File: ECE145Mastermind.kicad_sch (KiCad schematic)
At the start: 17 parts, among them U1 74LS148, U10 74LS76, U11 74LS76, U13 4053, U14 4053, U15 4051, U16 74LS161, U17 74HC00, U19 74HC00, U2 74LS194, U20 74HC00, U21 74LS139, U22 74LS08, U24 LM555xN, U26 74LS04, U29 74LS194, U30 74LS194

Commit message: Added FSM, Button, 555 timer, changed shift registers
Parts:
- added C1, C4: .01u, symbol Device:C
- added C2, C3: 1u, symbol Device:C
- added Q1: NMOS, symbol Simulation_SPICE:NMOS
- added R1: 1k, symbol Device:R
- added R2: 200k, symbol Device:R
- added R3, R4: R, symbol Device:R
- added SW1: SW_Push, symbol Switch:SW_Push
- added unit 5 of U1
- added unit 1 of U14
- added unit 5 of U14
- added U17: 40106, symbol 4xxx:40106
- added unit 3 of U2
- added U5: 74LS08, symbol 74xx:74LS08
- added unit 3 of U6
- added unit 3 of U8
- added unit 7 of U9
- U1: renamed from U20; value 74HC00 -> 74HCT00; symbol 74xx:74HC00 -> 74xx:74HCT00
- U1: renamed from U17; value 74HC00 -> 74HCT00; symbol 74xx:74HC00 -> 74xx:74HCT00
- U1: renamed from U19; value 74HC00 -> 74HCT00; symbol 74xx:74HC00 -> 74xx:74HCT00
- U15: renamed from U24; Name (none) -> 555 Timer
- U9: renamed from U26; value 74LS04 -> 74HCT04; symbol 74xx:74LS04 -> 74xx:74HCT04
- renumbered U13 to U10, U30 to U11, U14 to U12, U15 to U13, U22 to U14, U11 to U2, U29 to U3, U1 to U4, U10 to U6, U2 to U7, U21 to U8
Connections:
- net GND is gone; now on net +5V: U10.7 (VEE), U10.8 (VSS), U12.7 (VEE), U12.8 (VSS), U13.7 (VEE), U13.8 (VSS), U16.8 (GND), U4.8 (GND)
- net MUX.S is gone; now on net M: U10.10 (B), U10.11 (A), U10.9 (C), U12.9 (C)
- net Reset is gone; now on net GUESS: U2.2 (~{S}), U2.7 (~{S}), U6.2 (~{S}), U6.7 (~{S})
- net +5V: now also U10.6 (Inh), U11.10 (S1), U11.16 (VCC), U11.7 (Dsl), U11.8 (GND), U12.10 (B), U12.11 (A), U12.6 (Inh), U13.6 (Inh), U13.9 (C), U15.1 (GND), U15.4 (R), U15.8 (VCC), U16.10 (CET), U16.7 (CEP), U16.9 (~{PE}), U2.3 (~{R}), U2.4 (J), U2.8 (~{R}), U2.9 (J), U3.10 (S1), U3.16 (VCC), U3.8 (GND), U4.1 (I4), U4.2 (I5), U4.3 (I6), U4.4 (I7), U4.5 (EI), U6.3 (~{R}), U6.4 (J), U6.8 (~{R}), U6.9 (J), U7.10 (S1), U7.16 (VCC), U7.2 (Dsr), U7.8 (GND), C1.2, C2.2, C4.1, Q1.3 (S), R1.1, R3.1, R4.1, SW1.2, U1.14 (VCC), U1.7 (GND), U14.14 (VCC), U14.7 (GND), U17.14 (VDD), U17.7 (VSS), U2.13 (GND), U2.5 (VCC), U5.14 (VCC), U5.7 (GND), U6.13 (GND), U6.5 (VCC), U8.16 (VCC), U8.8 (GND), U9.14 (VCC), U9.7 (GND)
- net CLK: now also U11.11 (Cp), U15.3 (Q), U3.11 (Cp), U7.11 (Cp)
- net DONE: now also U14.6; no longer U14.3
- net M: now also U14.2
- net Out1: now also U11.3 (P0)
- net Out2: now also U11.4 (P1)
- net Out3: now also U1.10, U11.5 (P2); no longer U1.5
- net Out4: now also U1.13, U11.6 (P3); no longer U1.2
- net P: now also U11.9 (S0), U3.9 (S0)
- net S0: now also U14.4; no longer U14.1
- net S1: now also U14.5; no longer U14.2
- net at U10.12 (X0), U10.2 (Y0), U10.5 (Z0)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: now also Q1.1 (D)
- net GUESS: now reaches U16.1 (~{MR})
- net GUESS: now also U11.1 (Mr), U3.1 (Mr), U7.1 (Mr), U17.2
- net at U4.10 (IO): now also U1.11; no longer U1.3
- net at U4.11 (I1): now also U1.8; no longer U1.6
- net at U4.15 (EO): now also U3.2 (Dsr), U14.1
- net at U6.15 (Q): now also U1.12; no longer U1.1
- net at U15.2 (TR): now also U15.6 (THR), C2.1, R2.2
- net at U15.5 (CV): now also C1.1
- net at U15.7 (DIS): now also R1.2, R2.1
- net at U11.15 (Q0): now also Q1.2 (G)
- net at U7.9 (S0): now also U14.3
- net at U6.11 (Q): now also U1.9; no longer U1.4
- new net: C3.2, R4.2, U17.1
- new net: C3.1, C4.2, R3.2, SW1.1
- no-connect marks 0 -> 29
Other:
- sheet VoltageComparator renamed Voltage Comparator
- sheet VoltageComparator1 renamed Voltage Comparator1
- sheet VoltageComparator2 renamed Voltage Comparator2
- sheet VoltageComparator3 renamed Voltage Comparator3
- sheet FSM ports: added GUESS; removed none
- note added: "Consider Using CD4052 (dual 4-channel mux) when adding random codes"
- note added: "Misplaced Matches Shift Register"
- note added: "Perfect Matches Shift Register"
- title: (none) -> Mastermind Guess Checking

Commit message: slight tweaks
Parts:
- R3, R4: value R -> 10k
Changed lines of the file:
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@@
 			)
 		)
-		(property "Value" "R"
+		(property "Value" "10k"
 			(at 290.83 190.5 90)
 			(effects
@@
 			)
 		)
-		(property "Value" "R"
+		(property "Value" "10k"
 			(at 290.83 182.88 90)
 			(effects

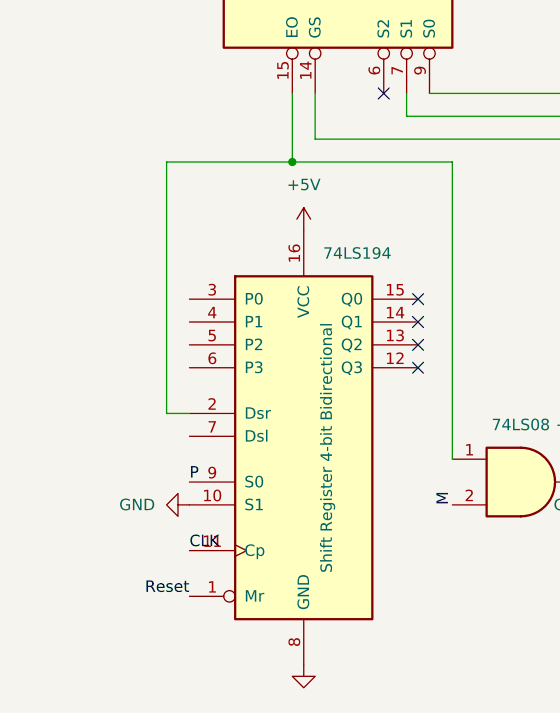
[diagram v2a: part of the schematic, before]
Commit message: Added AND gate for P shift register
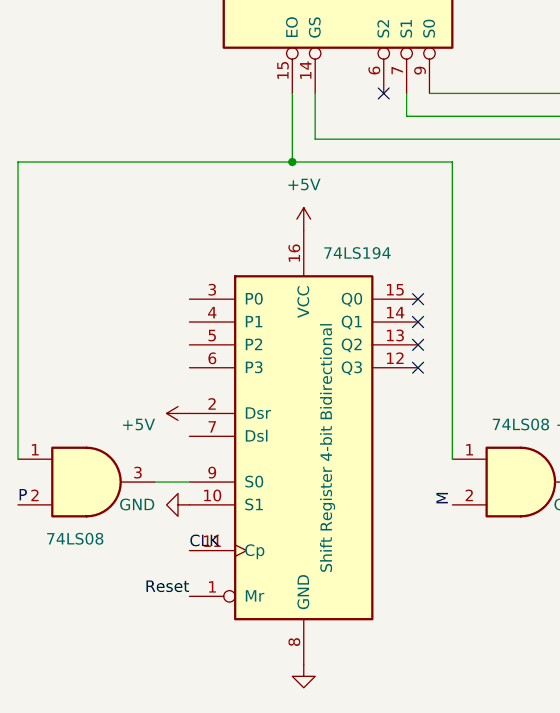
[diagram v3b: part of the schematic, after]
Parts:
- added U101: 74LS08, symbol 74xx:74LS08
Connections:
- net +5V: now also U3.2 (Dsr)
- net P: now also U101.2; no longer U3.9 (S0)
- net at U14.1, U4.15 (EO): now also U101.1; no longer U3.2 (Dsr)
- new net: U101.3, U3.9 (S0)
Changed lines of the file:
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@@
 	(wire
 		(pts
-			(xy 33.02 200.66) (xy 33.02 228.6)
+			(xy 16.51 200.66) (xy 16.51 233.68)
 		)
 		(stroke
@@
 	(wire
 		(pts
-			(xy 46.99 200.66) (xy 33.02 200.66)
+			(xy 46.99 200.66) (xy 16.51 200.66)
 		)
 		(stroke
@@
 	(wire
 		(pts
-			(xy 33.02 228.6) (xy 35.56 228.6)
-		)
-		(stroke
-			(width 0)
-			(type default)
-		)
-	)
-	(wire
-		(pts
 			(xy 53.34 135.89) (xy 53.34 144.78)
 		)
@@
 	(wire
 		(pts
+			(xy 31.75 236.22) (xy 35.56 236.22)
+		)
+		(stroke
+			(width 0)
+			(type default)
+		)
+	)
+	(wire
+		(pts
 			(xy 82.55 177.8) (xy 85.09 177.8)
 		)
@@
 		)
 	)
+	(label "P"
+		(at 16.51 238.76 0)
+		(effects
+			(font
+				(size 1.27 1.27)
+			)
+			(justify left bottom)
+		)
+	)
 	(label "S0"
 		(at 182.88 33.02 0)
@@
 		)
 	)
-	(label "P"
-		(at 35.56 236.22 0)
-		(effects
-			(font
-				(size 1.27 1.27)
-			)
-			(justify left bottom)
-		)
-	)
 	(label "Reset"
 		(at 83.82 248.92 180)
@@
 	)
 	(symbol
+		(lib_id "power:+5V")
+		(at 35.56 228.6 90)
+		(unit 1)
+		(exclude_from_sim no)
+		(in_bom yes)
+		(on_board yes)
+		(dnp no)
+		(fields_autoplaced yes)
+		(property "Reference" "#PWR0139"
+			(at 31.75 227.3299 90)
+			(effects
+				(font
+					(size 1.27 1.27)
+				)
+				(justify left)
+				(hide yes)
+			)
+		)
+		(property "Value" "+5V"
+			(at 31.75 229.8699 90)
+			(effects
+				(font
+					(size 1.27 1.27)
+				)
+				(justify left)
+			)
+		)
+		(property "Footprint" ""
+			(at 35.56 228.6 0)
+			(effects
+				(font
+					(size 1.27 1.27)
+				)
+				(hide yes)
+			)
+		)
+		(property "Datasheet" ""
+			(at 35.56 228.6 0)
+			(effects
+				(font
+					(size 1.27 1.27)
+				)
+				(hide yes)
+			)
+		)
+		(property "Description" "Power symbol creates a global label with name \"+5V\""
+			(at 35.56 228.6 0)
+			(effects
+				(font
+					(size 1.27 1.27)
+				)
+				(hide yes)
+			)
+		)
+		(pin "1"
+		)
+		(instances
+			(project "ECE145Mastermind"
+				(path "/8c64fe8a-5d6b-41bc-b3a3-9bda7b2e0f2c"
+					(reference "#PWR0139")
+					(unit 1)
+				)
+			)
+		)
+	)
+	(symbol
 		(lib_id "power:GND")
 		(at 48.26 256.54 0)
@@
 					(unit 1)
 				)
+			)
+		)
+	)
+	(symbol
+		(lib_id "74xx:74LS08")
+		(at 24.13 236.22 0)
+		(unit 1)
+		(exclude_from_sim no)
+		(in_bom yes)
+		(on_board yes)
+		(dnp no)
+		(property "Reference" "U101"
+			(at 24.1217 227.33 0)
+			(effects
+				(font
+					(size 1.27 1.27)
+				)
+				(hide yes)
+			)
+		)
+		(property "Value" "74LS08"
+			(at 22.86 242.57 0)
+			(effects
+				(font
+					(size 1.27 1.27)
+				)
+			)
+		)
+		(property "Footprint" ""
+			(at 24.13 236.22 0)
+			(effects
+				(font
+					(size 1.27 1.27)
+				)
+				(hide yes)
+			)
+		)
+		(property "Datasheet" "http://www.ti.com/lit/gpn/sn74LS08"
+			(at 24.13 236.22 0)
+			(effects
+				(font
+					(size 1.27 1.27)
+				)
+				(hide yes)
+			)
+		)
+		(property "Description" "Quad And2"
+			(at 24.13 236.22 0)
+			(effects
+				(font
+					(size 1.27 1.27)
+				)
+				(hide yes)
+			)
+		)
+		(pin "14"
+		)
+		(pin "7"
+		)
+		(pin "1"
+		)
+		(pin "6"
+		)
+		(pin "2"
+		)
+		(pin "3"
+		)
+		(pin "4"
+		)
+		(pin "5"
+		)
+		(pin "12"
+		)
+		(pin "13"
+		)
+		(pin "11"
+		)
+		(pin "9"
+		)
+		(pin "10"
+		)
+		(pin "8"
+		)
+		(instances
+			(project "ECE145Mastermind"
+				(path "/8c64fe8a-5d6b-41bc-b3a3-9bda7b2e0f2c"
+					(reference "U101")
+					(unit 1)
+				)

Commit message: Fixes
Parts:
- removed C3: 1u, symbol Device:C
- removed C4: .01u, symbol Device:C
- removed R3, R4: 10k, symbol Device:R
- removed SW1: SW_Push, symbol Switch:SW_Push
- removed unit 1 of U17
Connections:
- net +5V: no longer U12.10 (B)
- net G1: now also U10.5 (Z0); no longer U10.3 (Z1)
- net G2: now also U10.2 (Y0); no longer U10.1 (Y1)
- net G3: now also U12.5 (Z0); no longer U10.13 (X1)
- net G4: now also U12.2 (Y0); no longer U12.3 (Z1)
- net M: now also U12.10 (B)
- net VB3: now also U12.4 (Z); no longer U10.14 (X)
- net VB4: now also U12.15 (Y); no longer U12.4 (Z)
- net at U12.1 (Y1): now also Q1.1 (D), U10.1 (Y1), U10.3 (Z1), U12.3 (Z1), U13.3 (X)
- net GUESS renamed Reset
- now unconnected: U10.12 (X0)
- no-connect marks 29 -> 26
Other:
- sheet FSM ports: added Reset; removed GUESS

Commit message: Started PCB Work
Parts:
- removed U101: 74LS08, symbol 74xx:74LS08
- removed unit 1 of U14
- removed U2, U6: 74LS76, symbol 74xx:74LS76
- added C1, C10: 10u, Capacitor_SMD:C_0805_2012Metric_Pad1.18x1.45mm_HandSolder, symbol Device:C
- added C2, C3, C4, C5, C6, C7, C8, C9: .1u, Capacitor_SMD:C_0805_2012Metric_Pad1.18x1.45mm_HandSolder, symbol Device:C
- added J1: Conn_01x02_Socket, Connector_PinSocket_1.27mm:PinSocket_1x02_P1.27mm_Vertical, symbol Connector:Conn_01x02_Socket
- added R1, R2, R3: 10k, Resistor_SMD:R_0805_2012Metric_Pad1.20x1.40mm_HandSolder, symbol Device:R
- added SW1: SW_SPDT, Button_Switch_THT:SW_Slide_SPDT_Straight_CK_OS102011MS2Q, symbol Switch:SW_SPDT
- added unit 3 of U1
- added unit 1 of U1
- added unit 2 of U1
- added unit 6 of U10
- added unit 5 of U10
- added unit 2 of U10
- added unit 4 of U10
- added unit 3 of U10
- added U12: LM7805_TO220, Package_TO_SOT_THT:TO-220-3_Horizontal_TabDown, symbol Regulator_Linear:LM7805_TO220
- added U16: LM358, Package_SO:SOIC-8_3.9x4.9mm_P1.27mm, symbol Amplifier_Operational:LM358
- added U17, U18: LM324, Package_SO:SOIC-14_3.9x8.7mm_P1.27mm, symbol Amplifier_Operational:LM324
- added U22: 74HCT00, Package_SO:SOIC-14_3.9x8.7mm_P1.27mm, symbol 74xx:74HCT00
- added U3, U6: 74LS73, Package_SO:SOIC-14_3.9x8.7mm_P1.27mm, symbol 74xx:74LS73
- added unit 1 of U8
- added unit 7 of U9
- C11: renamed from C1; footprint (none) -> Capacitor_SMD:C_0805_2012Metric_Pad1.18x1.45mm_HandSolder
- C12: renamed from C2; footprint (none) -> Capacitor_SMD:C_0805_2012Metric_Pad1.18x1.45mm_HandSolder
- Q1: footprint (none) -> Package_TO_SOT_THT:TO-220-3_Horizontal_TabDown
- R4: renamed from R1; footprint (none) -> Resistor_SMD:R_0805_2012Metric_Pad1.20x1.40mm_HandSolder
- R5: renamed from R2; footprint (none) -> Resistor_SMD:R_0805_2012Metric_Pad1.20x1.40mm_HandSolder
- U1: renamed from U14; footprint (none) -> Package_SO:SOIC-14_3.9x8.7mm_P1.27mm
- U10: renamed from U17; footprint (none) -> Package_SO:SOIC-14_3.9x8.7mm_P1.27mm
- U11: renamed from U10; footprint (none) -> Package_SO:SOIC-16_3.9x9.9mm_P1.27mm
- U13: renamed from U11; footprint (none) -> Package_SO:SOIC-16_3.9x9.9mm_P1.27mm
- U14: renamed from U12; footprint (none) -> Package_SO:SOIC-16_3.9x9.9mm_P1.27mm
- U15: renamed from U13; footprint (none) -> Package_SO:SOIC-16_3.9x9.9mm_P1.27mm
- U19: renamed from U5; footprint (none) -> Package_SO:SOIC-14_3.9x8.7mm_P1.27mm
- U2: renamed from U1; footprint (none) -> Package_SO:SOIC-14_3.9x8.7mm_P1.27mm
- U20: renamed from U15; footprint Package_DIP:DIP-8_W7.62mm -> Package_SO:SOIC-8_3.9x4.9mm_P1.27mm
- U21: renamed from U16; footprint (none) -> Package_SO:SOIC-16_3.9x9.9mm_P1.27mm
- U4: renamed from U3; footprint (none) -> Package_SO:SOIC-16_3.9x9.9mm_P1.27mm
- U5: renamed from U4; footprint (none) -> Package_SO:SOIC-16_3.9x9.9mm_P1.27mm
- U7, U8: footprint (none) -> Package_SO:SOIC-16_3.9x9.9mm_P1.27mm
- U9: footprint (none) -> Package_SO:SOIC-14_3.9x8.7mm_P1.27mm
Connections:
- net +5V: now also C1.1, C10.1, C2.1, C3.1, C4.1, C5.1, C6.1, C7.1, C8.1, C9.1, R3.1, U12.3 (VO), U16.8 (V+), U17.4 (V+), U18.4 (V+), U3.4 (VCC), U6.4 (VCC), U9.14 (VCC); no longer C11.2, C12.2, Q1.3 (S), U1.7 (GND), U10.7 (VSS), U11.6 (Inh), U11.7 (VEE), U11.8 (VSS), U13.7 (Dsl), U13.8 (GND), U14.11 (A), U14.6 (Inh), U14.7 (VEE), U14.8 (VSS), U15.6 (Inh), U15.7 (VEE), U15.8 (VSS), U15.9 (C), U19.7 (GND), U2.7 (GND), U20.1 (GND), U21.8 (GND), U4.10 (S1), U4.2 (Dsr), U4.8 (GND), U5.5 (EI), U5.8 (GND), U7.10 (S1), U7.2 (Dsr), U7.8 (GND), U8.8 (GND), U9.14 (VCC), U9.7 (GND)
- net CLK: now also U9.13
- net DONE: now also U1.6; no longer U1.6
- net M: now also U7.7 (Dsl)
- net P: now also U4.7 (Dsl)
- net Reset: now also U1.10, U1.2, U3.2 (~{R}), U3.6 (~{R}), U6.2 (~{R}), U6.6 (~{R}); no longer U4.1 (Mr), U7.1 (Mr)
- net S0: now also U1.4; no longer U1.4
- net S1: now also U1.5; no longer U1.5
- net at U11.1 (Y1), U11.3 (Z1), U14.1 (Y1)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: now also U16.1, U16.2 (-); no longer Q1.1 (D), U15.3 (X)
- net at U2.4: now also U3.13 (~{Q})
- net at U9.1: now also U8.4 (O0); no longer U8.4 (O0)
- net at U2.1: now also U3.8 (~{Q})
- net at U9.5: now also U8.6 (O2); no longer U8.6 (O2)
- net at U5.15 (EO): now also U4.9 (S0), U7.9 (S0)
- net GND: now reaches U21.3 (D0)
- net GND: now also C11.2, C12.2, Q1.3 (S), U1.12, U1.13, U1.7 (GND), U10.7 (VSS), U11.6 (Inh), U11.7 (VEE), U11.8 (VSS), U13.2 (Dsr), U13.7 (Dsl), U13.8 (GND), U14.11 (A), U14.6 (Inh), U14.7 (VEE), U14.8 (VSS), U15.6 (Inh), U15.7 (VEE), U15.8 (VSS), U15.9 (C), U19.7 (GND), U2.7 (GND), U20.1 (GND), U21.4 (D1), U21.5 (D2), U21.6 (D3), U21.8 (GND), U4.10 (S1), U4.2 (Dsr), U4.3 (P0), U4.4 (P1), U4.5 (P2), U4.6 (P3), U4.8 (GND), U5.5 (EI), U5.8 (GND), U7.10 (S1), U7.2 (Dsr), U7.3 (P0), U7.4 (P1), U7.5 (P2), U7.6 (P3), U7.8 (GND), U8.13 (A1), U8.14 (A0), U8.15 (E), U8.8 (GND), C10.2, C2.2, C3.2, C4.2, C5.2, C6.2, C7.2, C8.2, C9.2, J1.2 (Pin_2), R1.2, R2.1, SW1.3 (C), U10.11, U10.13, U10.5, U10.9, U12.2 (GND), U16.4 (V-), U17.11 (V-), U18.11 (V-), U22.1, U22.2, U3.10 (K), U3.11 (GND), U3.3 (K), U6.10 (K), U6.11 (GND), U6.3 (K), U9.7 (GND)
- net at U5.14 (GS): now also U8.1 (E); no longer U8.1 (E)
- net at U5.7 (S1): now also U8.3 (A1); no longer U8.3 (A1)
- net at U5.9 (S0): now also U8.2 (A0); no longer U8.2 (A0)
- net at U2.12: now also U6.13 (~{Q})
- net at U9.3: now also U8.5 (O1); no longer U8.5 (O1)
- net at U9.9: now also U8.7 (O3); no longer U8.7 (O3)
- net Perfect LED/P4: now reaches U4.12 (Q3)
- net Perfect LED/P3: now reaches U4.13 (Q2)
- net Perfect LED/P2: now reaches U4.14 (Q1)
- net Perfect LED/P1: now reaches U4.15 (Q0)
- net Misplaced LED/M4: now reaches U7.12 (Q3)
- net Misplaced LED/M3: now reaches U7.13 (Q2)
- net Misplaced LED/M2: now reaches U7.14 (Q1)
- net Misplaced LED/M1: now reaches U7.15 (Q0)
- net at U2.9: now also U6.8 (~{Q})
- net K1 renamed J1
- net J1: now also U3.7 (J)
- net K2 renamed J2
- net J2: now also U3.14 (J)
- net K3 renamed J3
- net J3: now also U6.7 (J)
- net K4 renamed J4
- net J4: now also U6.14 (J)
- new net: C1.2, R1.1, U10.3
- new net: Q1.1 (D), U15.3 (X), U16.3 (+)
- new net: U1.8, U7.1 (Mr)
- new net: U1.3, U4.1 (Mr)
- new net: R2.2, R3.2, U16.5 (+)
- new net: U16.6 (-), U16.7
- new net: J1.1 (Pin_1), SW1.1 (A)
- new net: SW1.2 (B), U12.1 (VI)
- new net PWR_ON_RST: U1.1, U1.9, U10.4
- new net ~{CLK}: U3.1 (C), U3.5 (C), U6.1 (C), U6.5 (C), U9.12
- no-connect marks 26 -> 31
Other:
- added sheet Misplaced LED (Misplaced LED.kicad_sch)
- added sheet Perfect LED (Perfect LED.kicad_sch)
- note added: "TIE ALL UNUSED INPUTS LOW"
- note added: "Unused IC Units"
- note removed: "Consider Using CD4052 (dual 4-channel mux) when adding random codes"

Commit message: For Sharvesh
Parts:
- removed unit 3 of U1
- added D9: LED, LED_SMD:LED_0805_2012Metric_Pad1.15x1.40mm_HandSolder, symbol Device:LED
- added R32: 1k, Resistor_SMD:R_0805_2012Metric_Pad1.20x1.40mm_HandSolder, symbol Device:R
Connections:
- net +5V: now also R32.1
- net GND: now also U1.10, U1.9, D9.1 (K)
- net at U7.1 (Mr): now also U1.3, U4.1 (Mr)
- new net: D9.2 (A), R32.2
- no-connect marks 31 -> 32
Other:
- moved on the sheet: U1C

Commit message: routed
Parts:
- added unit 1 of U1
- C12: value 1u -> .1u
- R6: renamed from R5; value 200k -> 10k
- renumbered D9 to D1, R32 to R1, R1 to R2, R2 to R3, R3 to R4, R4 to R5, U6 to U3, U3 to U6
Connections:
- net GND: now also U22.4, U22.5, U4.7 (Dsl), U7.7 (Dsl); no longer U22.1, U22.2, U4.2 (Dsr), U7.2 (Dsr)
- net M: now also U7.2 (Dsr); no longer U7.7 (Dsl)
- net Out1: now also U2.13; no longer U2.2
- net Out2: now also U2.9; no longer U2.5
- net Out3: now also U2.5; no longer U2.10
- net Out4: now also U2.2; no longer U2.13
- net P: now also U4.2 (Dsr); no longer U4.7 (Dsl)
- net PWR_ON_RST: now also U10.2, U1.1; no longer U1.1, U10.4
- net Reset: now also U1.2; no longer U1.2
- net at C1.2, R2.1: now also U10.1; no longer U10.3
- net at U15.3 (X), U16.3 (+): now also Q1.2 (D); no longer Q1.1 (D)
- net at U3.13 (~{Q}): now also U2.1; no longer U2.12
- net at U6.13 (~{Q}): now also U2.10; no longer U2.4
- net at U5.12 (I2): now also U2.8; no longer U2.6
- net at U3.8 (~{Q}): now also U2.4; no longer U2.9
- net at U5.10 (IO): now also U2.3; no longer U2.11
- net at U5.11 (I1): now also U2.6; no longer U2.8
- net at U5.13 (I3): now also U2.11; no longer U2.3
- net at U4.1 (Mr), U7.1 (Mr): now also U1.3; no longer U1.3
- net at U13.15 (Q0): now also Q1.1 (G); no longer Q1.2 (G)
- net at U6.8 (~{Q}): now also U2.12; no longer U2.1
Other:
- moved on the sheet: U2C

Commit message: Ground and Power Plane?
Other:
- sheet Voltage Comparator1: file VoltageComparator.kicad_sch -> VoltageComparator2.kicad_sch
- sheet Voltage Comparator2: file VoltageComparator.kicad_sch -> VoltageComparator3.kicad_sch
- sheet Voltage Comparator3: file VoltageComparator.kicad_sch -> VoltageComparator4.kicad_sch
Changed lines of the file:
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@@
 			)
 		)
-		(property "Sheetfile" "VoltageComparator.kicad_sch"
+		(property "Sheetfile" "VoltageComparator3.kicad_sch"
 			(at 73.66 121.2346 0)
 			(effects
@@
 			)
 		)
-		(property "Sheetfile" "VoltageComparator.kicad_sch"
+		(property "Sheetfile" "VoltageComparator2.kicad_sch"
 			(at 52.07 121.2346 0)
 			(effects
@@
 			)
 		)
-		(property "Sheetfile" "VoltageComparator.kicad_sch"
+		(property "Sheetfile" "VoltageComparator4.kicad_sch"
 			(at 95.25 121.2346 0)
 			(effects
